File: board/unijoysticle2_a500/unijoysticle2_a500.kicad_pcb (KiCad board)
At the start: 4 copper layers, 67 x 52 mm, 54 parts, among them J1 USB_B_Micro, J2 PORT JOY #1, J3 PORT JOY #2, Q1 S8050, Q2 S8050, SW1 RESET, SW2 BOOT, SW3 MOUSE, SW4 SWAP, U1 ESP32-WROOM-32E, U2 AMS1117-3.3, U3 CH340C, U4 74HC05, U5 74HC05, U6 74HC05

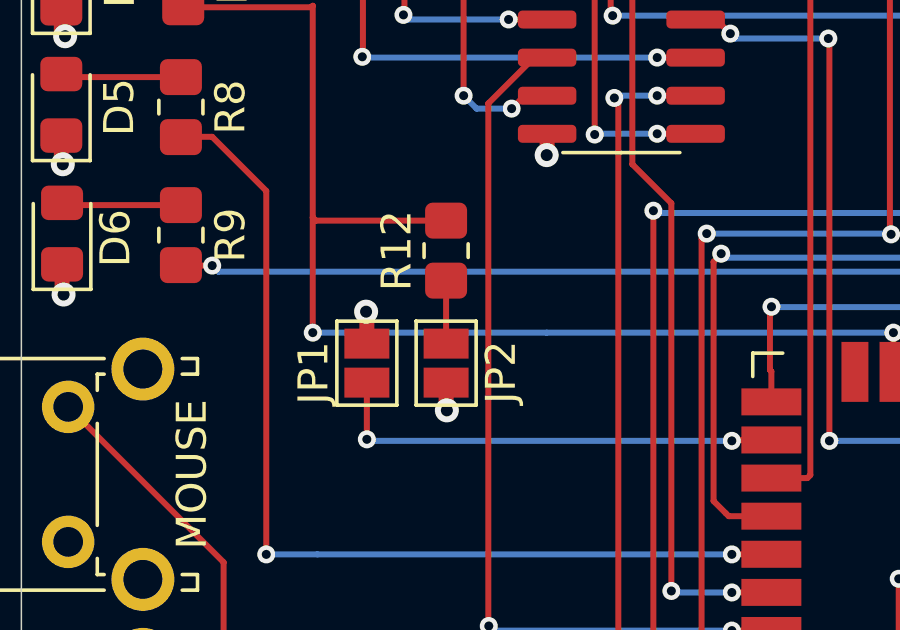
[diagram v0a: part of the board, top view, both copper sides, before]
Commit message: Uni 2 A500 Rev B:
- Cap 1500uF instead of 1000uF
- Use Resister 0 (R15) instead of JP2. Back resistor for JP2 2.2K
- LED resistors to be 2.2K
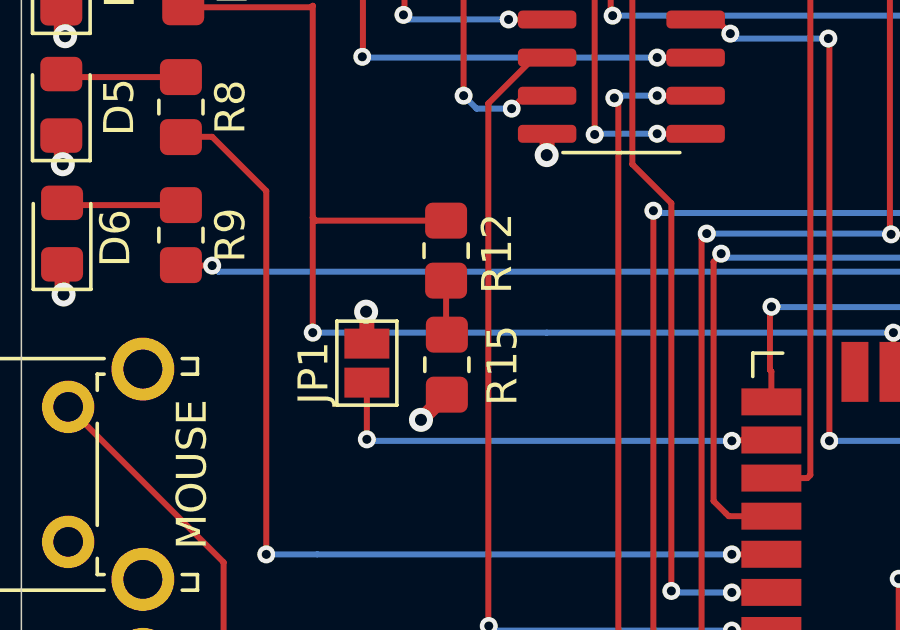
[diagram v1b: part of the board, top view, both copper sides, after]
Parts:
- removed JP2: SolderJumper_2_Open, Jumper:SolderJumper-2_P1.3mm_Open_Pad1.0x1.5mm
- added R15: 0, Resistor_SMD:R_0805_2012Metric_Pad1.20x1.40mm_HandSolder, F.Cu at (94.2, 122.5)
- C6: value 1000uF -> 1500uF
- R12: value 1K -> 2.2K
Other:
- board text added: "Unijoysticle 2 A500 Rev. B"
- board text removed: "Unijoysticle 2 A500 Rev. A"
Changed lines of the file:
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@@
   (title_block
     (title "Unijoysticle 2 A500")
-    (date "2022-04-25")
-    (rev "A")
+    (date "2022-05-15")
+    (rev "B")
     (company "Retro Moe")
   )
@@
   (net 73 "GPIO_BOOTSTRAP_15_LED_BT")
   (net 74 "GPIO_36")
-  (net 75 "Net-(JP2-Pad2)")
+  (net 75 "Net-(R12-Pad1)")
   (net 76 "unconnected-(U4-Pad12)")
   (net 77 "unconnected-(U4-Pad13)")
@@
     )
   )
-  (footprint "Jumper:SolderJumper-2_P1.3mm_Open_Pad1.0x1.5mm" (layer "F.Cu")
-    (at 94.1578 122.4534 90)
-    (descr "SMD Solder Jumper, 1x1.5mm Pads, 0.3mm gap, open")
-    (tags "solder jumper open")
-    (property "Sheetfile" "amiga_ports.kicad_sch")
-    (property "Sheetname" "Amiga Ports")
-    (attr exclude_from_pos_files)
-    (fp_text reference "JP2" (at -0.3048 1.8288 90) (layer "F.SilkS")
-      (effects (font (size 1 1) (thickness 0.15)))
-    )
-    (fp_text value "SolderJumper_2_Open" (at 0 1.9 90) (layer "F.Fab")
-      (effects (font (size 1 1) (thickness 0.15)))
-    )
-    (fp_line (start 1.4 1) (end -1.4 1) (layer "F.SilkS") (width 0.12))
-    (fp_line (start -1.4 1) (end -1.4 -1) (layer "F.SilkS") (width 0.12))
-    (fp_line (start -1.4 -1) (end 1.4 -1) (layer "F.SilkS") (width 0.12))
-    (fp_line (start 1.4 -1) (end 1.4 1) (layer "F.SilkS") (width 0.12))
-    (fp_line (start 1.65 1.25) (end -1.65 1.25) (layer "F.CrtYd") (width 0.05))
-    (fp_line (start 1.65 1.25) (end 1.65 -1.25) (layer "F.CrtYd") (width 0.05))
-    (fp_line (start -1.65 -1.25) (end 1.65 -1.25) (layer "F.CrtYd") (width 0.05))
-    (fp_line (start -1.65 -1.25) (end -1.65 1.25) (layer "F.CrtYd") (width 0.05))
-    (pad "1" smd rect (at -0.65 0 90) (size 1 1.5) (layers "F.Cu" "F.Mask")
-      (net 72 "GND") (pinfunction "A") (pintype "passive"))
-    (pad "2" smd rect (at 0.65 0 90) (size 1 1.5) (layers "F.Cu" "F.Mask")
-      (net 75 "Net-(JP2-Pad2)") (pinfunction "B") (pintype "passive"))
-  )
   (footprint "Resistor_SMD:R_0805_2012Metric_Pad1.20x1.40mm_HandSolder" (layer "F.Cu")
     (at 94.1578 118.7036 90)
@@
     (property "Sheetname" "Amiga Ports")
     (attr smd)
-    (fp_text reference "R12" (at 0 -1.65 90) (layer "F.SilkS")
+    (fp_text reference "R12" (at -0.0922 1.7018 90) (layer "F.SilkS")
       (effects (font (size 1 1) (thickness 0.15)))
     )
-    (fp_text value "1K" (at 0 1.65 90) (layer "F.Fab")
+    (fp_text value "2.2K" (at -0.0668 3.1242 90) (layer "F.Fab")
       (effects (font (size 1 1) (thickness 0.15)))
     )
@@
     (fp_line (start -1 -0.625) (end 1 -0.625) (layer "F.Fab") (width 0.1))
     (pad "1" smd roundrect (at -1 0 90) (size 1.2 1.4) (layers "F.Cu" "F.Paste" "F.Mask") (roundrect_rratio 0.2083333333)
-      (net 75 "Net-(JP2-Pad2)") (pintype "passive"))
+      (net 75 "Net-(R12-Pad1)") (pintype "passive"))
     (pad "2" smd roundrect (at 1 0 90) (size 1.2 1.4) (layers "F.Cu" "F.Paste" "F.Mask") (roundrect_rratio 0.2083333333)
       (net 73 "GPIO_BOOTSTRAP_15_LED_BT") (pintype "passive"))
@@
       (effects (font (size 1 1) (thickness 0.15)))
     )
-    (fp_text value "1000uF" (at 0 6.2 90) (layer "F.Fab")
+    (fp_text value "1500uF" (at 0 6.2 90) (layer "F.Fab")
       (effects (font (size 1 1) (thickness 0.15)))
     )
@@
     )
   )
+  (footprint "Resistor_SMD:R_0805_2012Metric_Pad1.20x1.40mm_HandSolder" (layer "F.Cu")
+    (at 94.1832 122.5042 90)
+    (descr "Resistor SMD 0805 (2012 Metric), square (rectangular) end terminal, IPC_7351 nominal with elongated pad for handsoldering. (Body size source: IPC-SM-782 page 72, https://www.pcb-3d.com/wordpress/wp-content/uploads/ipc-sm-782a_amendment_1_and_2.pdf), generated with kicad-footprint-generator")
+    (tags "resistor handsolder")
+    (property "Sheetfile" "amiga_ports.kicad_sch")
+    (property "Sheetname" "Amiga Ports")
+    (attr smd)
+    (fp_text reference "R15" (at -0.0254 1.8542 90) (layer "F.SilkS")
+      (effects (font (size 1 1) (thickness 0.15)))
+    )
+    (fp_text value "0" (at 0.1778 3.1496 90) (layer "F.Fab")
+      (effects (font (size 1 1) (thickness 0.15)))
+    )
+    (fp_text user "${REFERENCE}" (at 0 0 90) (layer "F.Fab")
+      (effects (font (size 0.5 0.5) (thickness 0.08)))
+    )
+    (fp_line (start -0.227064 -0.735) (end 0.227064 -0.735) (layer "F.SilkS") (width 0.12))
+    (fp_line (start -0.227064 0.735) (end 0.227064 0.735) (layer "F.SilkS") (width 0.12))
+    (fp_line (start -1.85 -0.95) (end 1.85 -0.95) (layer "F.CrtYd") (width 0.05))
+    (fp_line (start -1.85 0.95) (end -1.85 -0.95) (layer "F.CrtYd") (width 0.05))
+    (fp_line (start 1.85 -0.95) (end 1.85 0.95) (layer "F.CrtYd") (width 0.05))
+    (fp_line (start 1.85 0.95) (end -1.85 0.95) (layer "F.CrtYd") (width 0.05))
+    (fp_line (start -1 -0.625) (end 1 -0.625) (layer "F.Fab") (width 0.1))
+    (fp_line (start 1 -0.625) (end 1 0.625) (layer "F.Fab") (width 0.1))
+    (fp_line (start 1 0.625) (end -1 0.625) (layer "F.Fab") (width 0.1))
+    (fp_line (start -1 0.625) (end -1 -0.625) (layer "F.Fab") (width 0.1))
+    (pad "1" smd roundrect (at -1 0 90) (size 1.2 1.4) (layers "F.Cu" "F.Paste" "F.Mask") (roundrect_rratio 0.208333)
+      (net 72 "GND") (pintype "passive"))
+    (pad "2" smd roundrect (at 1 0 90) (size 1.2 1.4) (layers "F.Cu" "F.Paste" "F.Mask") (roundrect_rratio 0.208333)
+      (net 75 "Net-(R12-Pad1)") (pintype "passive"))
+    (model "${KICAD6_3DMODEL_DIR}/Resistor_SMD.3dshapes/R_0805_2012Metric.wrl"
+      (offset (xyz 0 0 0))
+      (scale (xyz 1 1 1))
+      (rotate (xyz 0 0 0))
+    )
+  )
   (footprint "Capacitor_SMD:C_0805_2012Metric_Pad1.18x1.45mm_HandSolder" (layer "F.Cu")
     (at 115.2906 104.7496)
@@
     (effects (font (size 1.5 1.5) (thickness 0.3)) (justify mirror))
   )
-  (gr_text "Unijoysticle 2 A500\nRev. A" (at 113.62 131.185) (layer "B.SilkS")
+  (gr_text "Unijoysticle 2 A500\nRev. B" (at 113.62 131.185) (layer "B.SilkS")
     (effects (font (size 1.5 1.5) (thickness 0.3)) (justify mirror))
   )
@@
   (segment (start 95.5763 140.6652) (end 95.5763 139.5437) (width 0.5) (layer "F.Cu") (net 72))
   (segment (start 123.1001 114.81) (end 122.936 114.9741) (width 0.5) (layer "F.Cu") (net 72))
+  (segment (start 94.1601 123.5042) (end 93.3196 124.3447) (width 0.5) (layer "F.Cu") (net 72))
   (segment (start 81.3308 115.7732) (end 81.3816 115.824) (width 0.5) (layer "F.Cu") (net 72))
   (segment (start 134.3191 121.0564) (end 133.9342 121.0564) (width 0.5) (layer "F.Cu") (net 72))
@@
   (segment (start 97.525 114.81) (end 97.525 115.5048) (width 0.5) (layer "F.Cu") (net 72))
   (segment (start 126.6416 117.9114) (end 127.5034 117.9114) (width 0.5) (layer "F.Cu") (net 72))
+  (segment (start 94.1832 123.5042) (end 94.1601 123.5042) (width 0.5) (layer "F.Cu") (net 72))
   (segment (start 129.9679 104.4995) (end 130.7084 103.759) (width 0.5) (layer "F.Cu") (net 72))
   (segment (start 138.7344 118.7564) (end 138.7344 117.627) (width 0.5) (layer "F.Cu") (net 72))
-  (segment (start 94.1578 124.0028) (end 94.1832 124.0282) (width 0.5) (layer "F.Cu") (net 72))
   (segment (start 140.2984 128.1064) (end 140.2842 128.0922) (width 0.5) (layer "F.Cu") (net 72))
   (segment (start 98.171 147.0496) (end 97.3164 147.0496) (width 0.5) (layer "F.Cu") (net 72))
@@
   (segment (start 143.256 144.0942) (end 145.796 141.5542) (width 0.5) (layer "F.Cu") (net 72))
   (segment (start 91.5162 120.7633) (end 91.4908 120.7379) (width 0.5) (layer "F.Cu") (net 72))
-  (segment (start 94.1578 123.1034) (end 94.1578 124.0028) (width 0.5) (layer "F.Cu") (net 72))
   (segment (start 140.5128 105.1692) (end 138.8496 105.1692) (width 0.5) (layer "F.Cu") (net 72))
   (segment (start 119.215 121.577) (end 119.253 121.539) (width 0.5) (layer "F.Cu") (net 72))
@@
   (via (at 91.4908 120.7379) (size 0.8) (drill 0.4) (layers "F.Cu" "B.Cu") (net 72))
   (via (at 131.628947 139.426747) (size 0.8) (drill 0.4) (layers "F.Cu" "B.Cu") (net 72))
-  (via (at 94.1832 124.0282) (size 0.8) (drill 0.4) (layers "F.Cu" "B.Cu") (net 72))
   (via (at 110.5916 115.5446) (size 0.8) (drill 0.4) (layers "F.Cu" "B.Cu") (net 72))
+  (via (at 93.3196 124.3447) (size 0.8) (drill 0.4) (layers "F.Cu" "B.Cu") (net 72))
   (via (at 127.508 117.9068) (size 0.8) (drill 0.4) (layers "F.Cu" "B.Cu") (net 72))
   (via (at 127.2286 136.4742) (size 0.8) (drill 0.4) (layers "F.Cu" "B.Cu") (net 72))
@@
   (segment (start 99.8728 136.7028) (end 100.040511 136.870511) (width 0.2) (layer "B.Cu") (net 74))
   (segment (start 98.4758 136.7028) (end 99.8728 136.7028) (width 0.2) (layer "B.Cu") (net 74))
-  (segment (start 94.1578 121.8034) (end 94.1578 119.7036) (width 0.2) (layer "F.Cu") (net 75))
+  (segment (start 94.1578 119.7036) (end 94.1578 121.4788) (width 0.2) (layer "F.Cu") (net 75))
+  (segment (start 94.1578 121.4788) (end 94.1832 121.5042) (width 0.2) (layer "F.Cu") (net 75))
   (zone (net 72) (net_name "GND") (layer "In1.Cu") (hatch edge 0.508)
     (connect_pads (clearance 0.508))

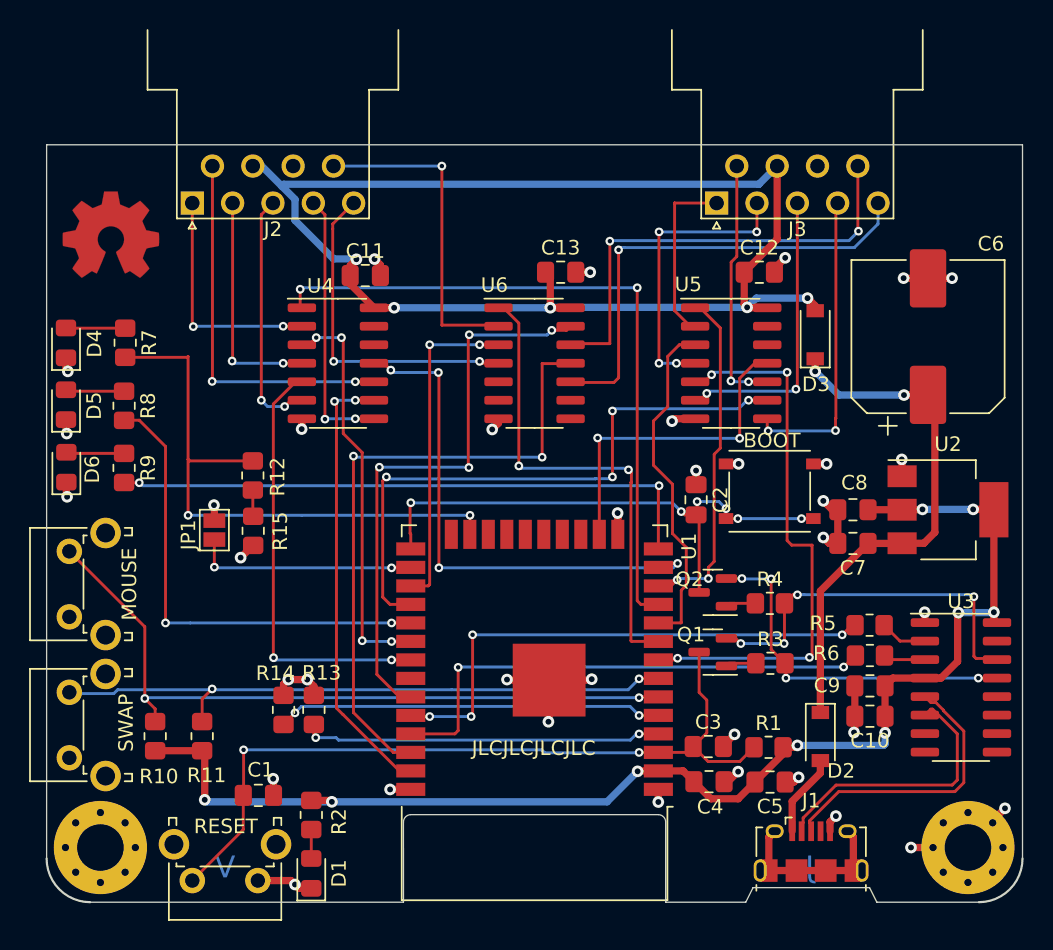
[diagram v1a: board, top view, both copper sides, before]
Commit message: Uni2 A500: CH340 powered by VBUS
Instead of powering CH340 from V3, power it from VBUS.
This should help, when the device is powered by the Amiga, it should not
power the CH340.

Not tested.
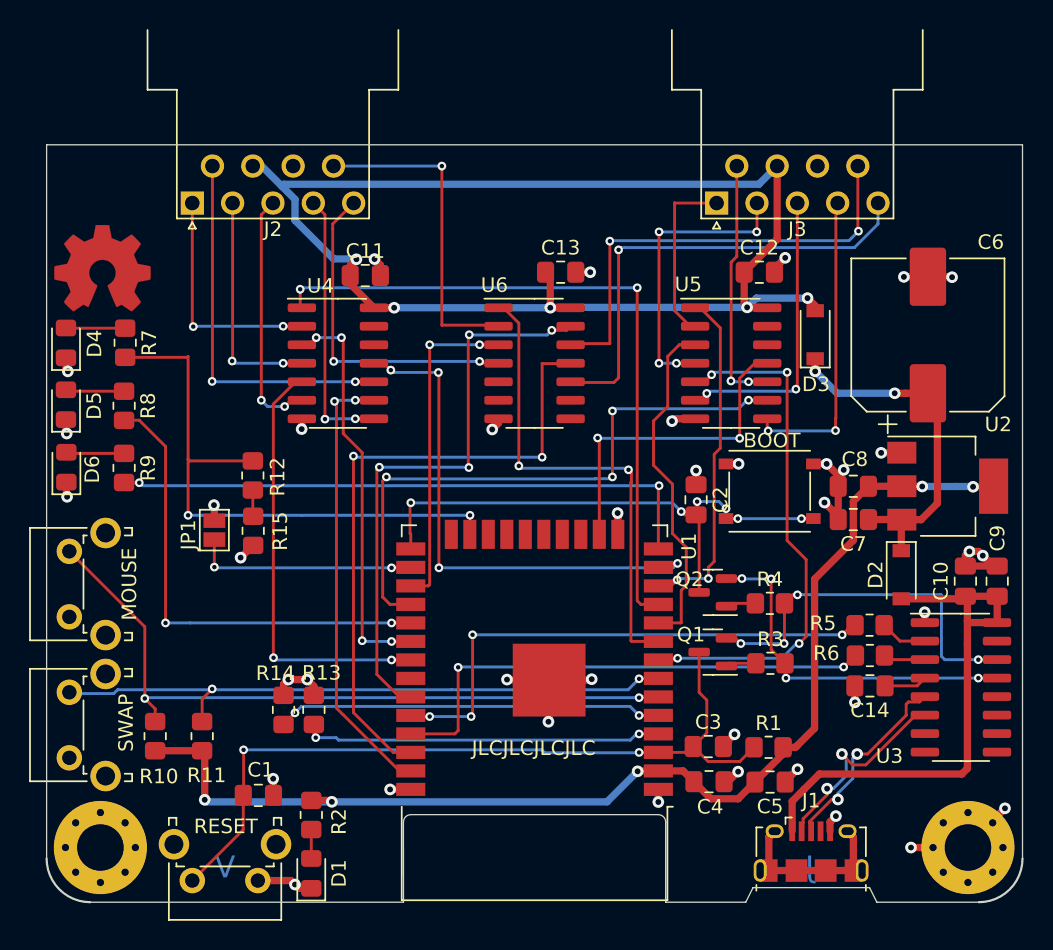
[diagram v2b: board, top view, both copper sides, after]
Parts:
- added C14: .1uF, Capacitor_SMD:C_0805_2012Metric_Pad1.18x1.45mm_HandSolder, F.Cu at (136.5, 133.1)
- R2, R7, R8, R9: value 1.5K -> 2.2K
- moved D2 12.4 mm to (138.7, 125.5)
- moved C10 11.4 mm to (143.1, 126.0), turned to 90 degrees
- moved C9 11.3 mm to (145.3, 126.0), turned to 90 degrees
- moved REF** 2.38 mm to (83.8, 104.5)
- moved C7 1.64 mm to (135.4, 121.7)
- moved U2 1.62 mm to (141.9, 119.4)
- moved C8 1.61 mm to (135.4, 119.4)
- moved C6 0.11 mm to (140.5, 109.1)
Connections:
- C10 pad 1: +3V3 -> VBUS
- C9 pad 1: +3V3 -> VBUS
- U3 pad 16: +3V3 -> VBUS
- U3 pad 4: +3V3 -> Net-(U3-Pad4)
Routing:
- net VBUS: track 5.65 -> 37.5 mm
- net Net-(C6-Pad1): track 36.8 -> 24.4 mm
- net +3V3: track 90.6 -> 81.0 mm, vias 9 -> 5
- net /USB Serial & Power/USBD+: track 19.6 -> 13.7 mm, vias 0 -> 2
- net GND: track 60.1 -> 65.6 mm, vias 37 -> 39
- net /USB Serial & Power/USBD-: track 18.9 -> 14.4 mm, vias 0 -> 2
- net Net-(U3-Pad4): track 0.00 -> 2.96 mm
- net GPIO_J2_LEFT: track 38.2 -> 36.1 mm
